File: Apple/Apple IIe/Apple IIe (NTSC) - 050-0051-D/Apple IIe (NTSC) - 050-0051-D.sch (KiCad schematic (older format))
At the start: 0 parts

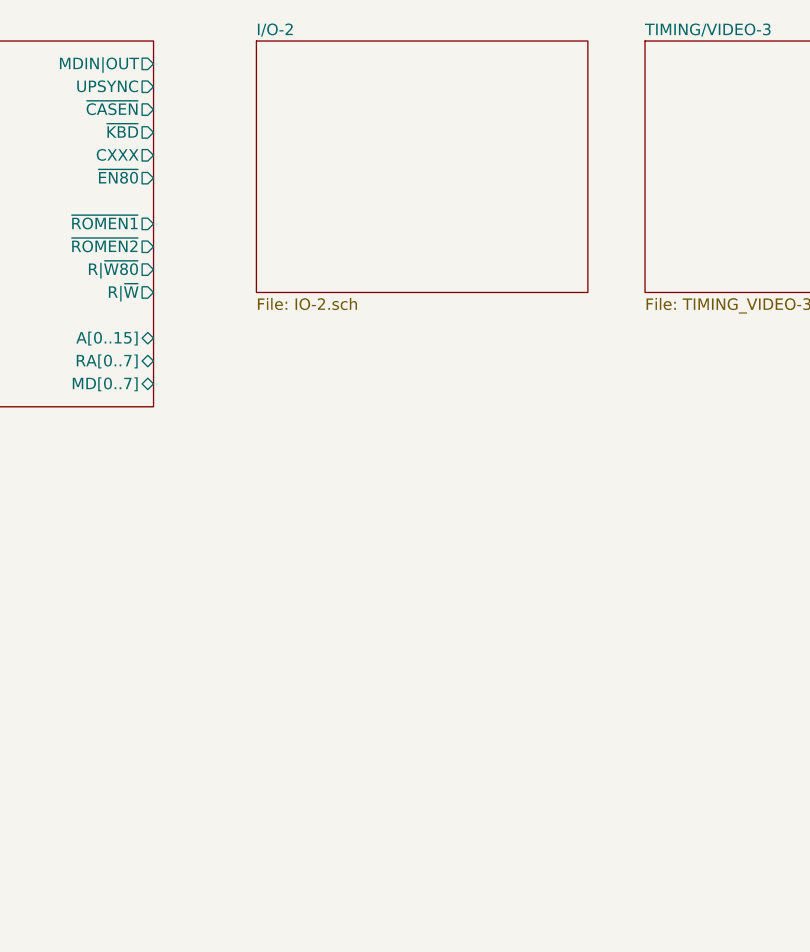
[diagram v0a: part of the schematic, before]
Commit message: Rough pass at I/O sheet
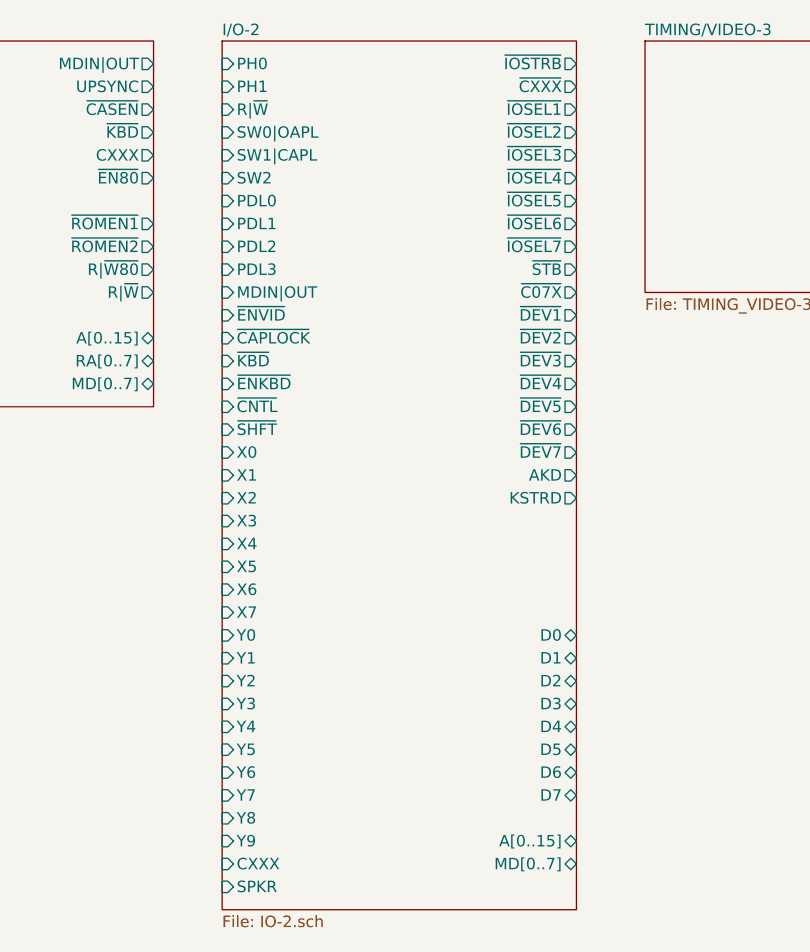
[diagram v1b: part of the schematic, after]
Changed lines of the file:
@@
 $EndSheet
 $Sheet
-S 3800 2800 1450 1100
+S 3650 2800 1550 3800
 U 60B91331
 F0 "I/O-2" 50
 F1 "IO-2.sch" 50
+F2 "SW2" I L 3650 3400 50
+F3 "SW1|CAPL" I L 3650 3300 50
+F4 "SW0|OAPL" I L 3650 3200 50
+F5 "~IOSTRB" O R 5200 2900 50
+F6 "~CXXX" O R 5200 3000 50
+F7 "~IOSEL1" O R 5200 3100 50
+F8 "~IOSEL2" O R 5200 3200 50
+F9 "~IOSEL3" O R 5200 3300 50
+F10 "~IOSEL4" O R 5200 3400 50
+F11 "~IOSEL5" O R 5200 3500 50
+F12 "~IOSEL6" O R 5200 3600 50
+F13 "~IOSEL7" O R 5200 3700 50
+F14 "~STB" O R 5200 3800 50
+F15 "~C07X" O R 5200 3900 50
+F16 "~DEV1" O R 5200 4000 50
+F17 "~DEV2" O R 5200 4100 50
+F18 "~DEV3" O R 5200 4200 50
+F19 "~DEV4" O R 5200 4300 50
+F20 "~DEV5" O R 5200 4400 50
+F21 "~DEV6" O R 5200 4500 50
+F22 "~DEV7" O R 5200 4600 50
+F23 "PDL0" I L 3650 3500 50
+F24 "PDL1" I L 3650 3600 50
+F25 "PDL2" I L 3650 3700 50
+F26 "PDL3" I L 3650 3800 50
+F27 "PH0" I L 3650 2900 50
+F28 "R|~W" I L 3650 3100 50
+F29 "MDIN|OUT" I L 3650 3900 50
+F30 "~ENVID" I L 3650 4000 50
+F31 "~CAPLOCK" I L 3650 4100 50
+F32 "~KBD" I L 3650 4200 50
+F33 "~ENKBD" I L 3650 4300 50
+F34 "~CNTL" I L 3650 4400 50
+F35 "~SHFT" I L 3650 4500 50
+F36 "X7" I L 3650 5300 50
+F37 "X6" I L 3650 5200 50
+F38 "X5" I L 3650 5100 50
+F39 "X4" I L 3650 5000 50
+F40 "X3" I L 3650 4900 50
+F41 "X2" I L 3650 4800 50
+F42 "X1" I L 3650 4700 50
+F43 "X0" I L 3650 4600 50
+F44 "Y9" I L 3650 6300 50
+F45 "Y8" I L 3650 6200 50
+F46 "Y7" I L 3650 6100 50
+F47 "Y6" I L 3650 6000 50
+F48 "Y5" I L 3650 5900 50
+F49 "Y4" I L 3650 5800 50
+F50 "Y3" I L 3650 5700 50
+F51 "Y2" I L 3650 5600 50
+F52 "Y1" I L 3650 5500 50
+F53 "Y0" I L 3650 5400 50
+F54 "AKD" O R 5200 4700 50
+F55 "KSTRD" O R 5200 4800 50
+F56 "MD[0..7]" B R 5200 6400 50
+F57 "A[0..15]" B R 5200 6300 50
+F58 "PH1" I L 3650 3000 50
+F59 "CXXX" I L 3650 6400 50
+F60 "D0" B R 5200 5400 50
+F61 "D1" B R 5200 5500 50
+F62 "D2" B R 5200 5600 50
+F63 "D3" B R 5200 5700 50
+F64 "D4" B R 5200 5800 50
+F65 "D5" B R 5200 5900 50
+F66 "D6" B R 5200 6000 50
+F67 "D7" B R 5200 6100 50
+F68 "SPKR" I L 3650 6500 50
 $EndSheet
 $Sheet

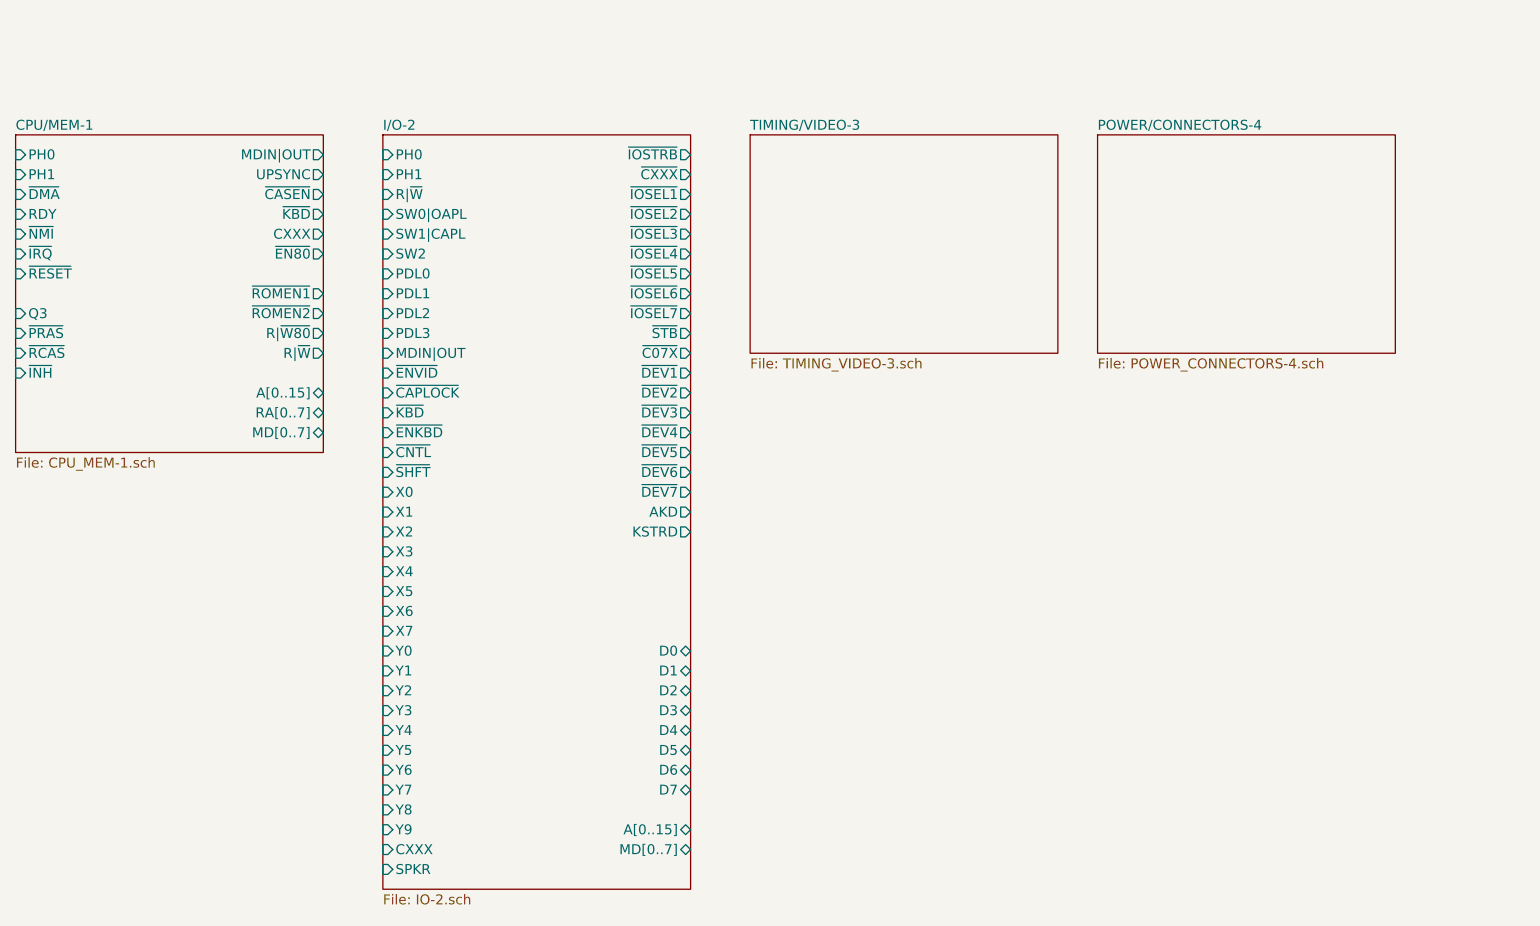
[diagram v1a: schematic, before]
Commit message: Rough pass at TIMING/VIDEO sheet
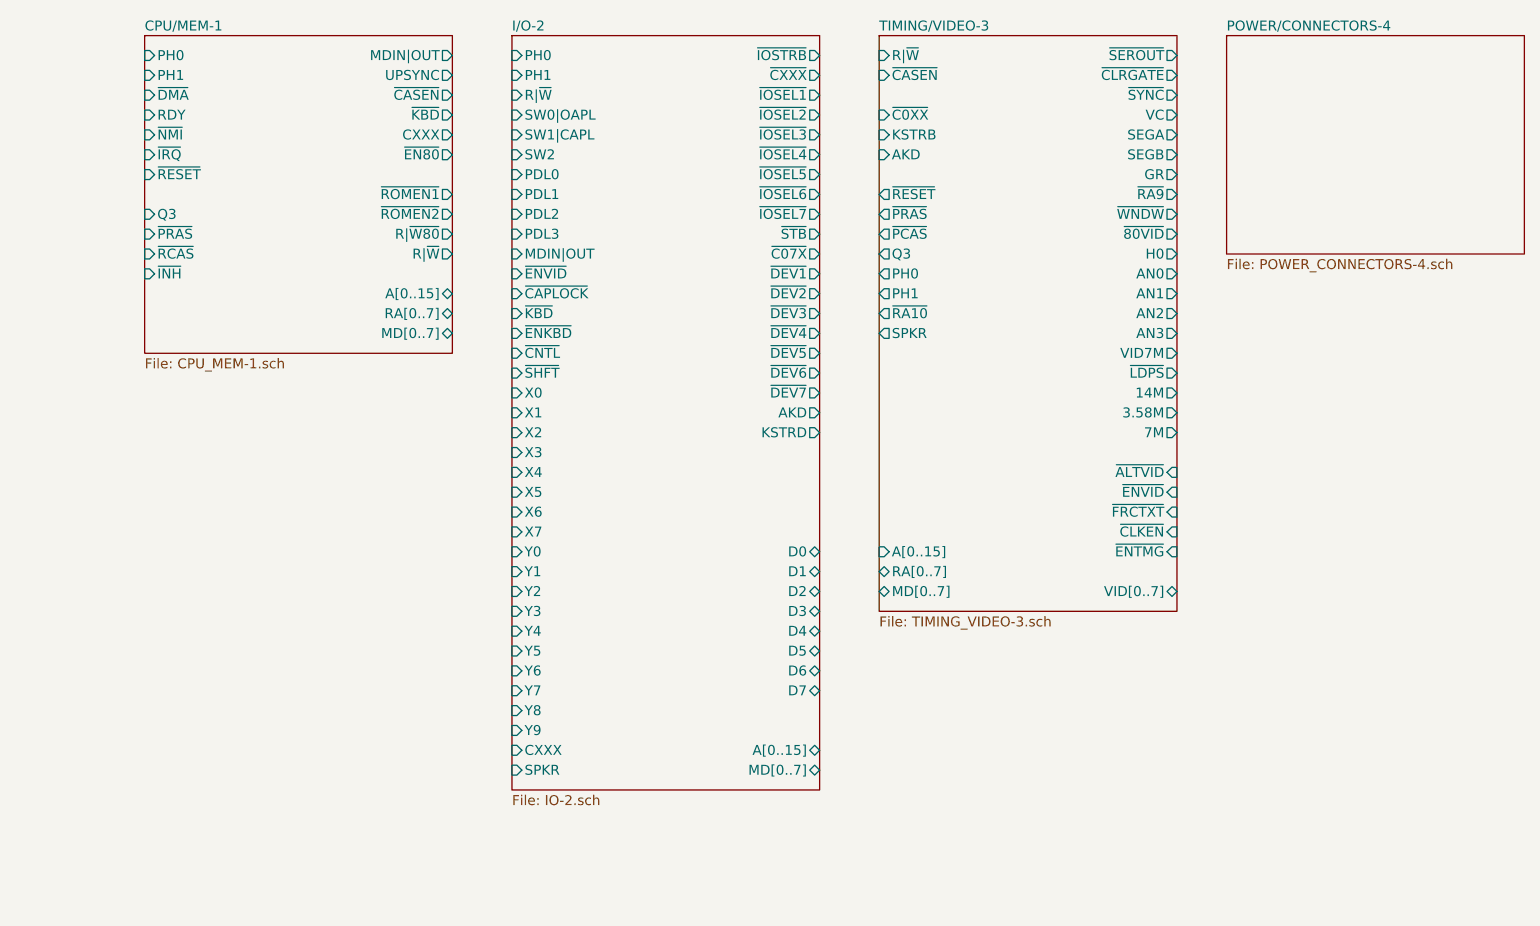
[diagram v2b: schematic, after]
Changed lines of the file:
@@
 $EndDescr
 $Sheet
-S 1800 2800 1550 1600
+S 2450 2300 1550 1600
 U 60B912AE
 F0 "CPU/MEM-1" 50
 F1 "CPU_MEM-1.sch" 50
-F2 "~RESET" I L 1800 3500 50
-F3 "~IRQ" I L 1800 3400 50
-F4 "~NMI" I L 1800 3300 50
-F5 "RDY" I L 1800 3200 50
-F6 "~DMA" I L 1800 3100 50
-F7 "RA[0..7]" B R 3350 4200 50
-F8 "PH0" I L 1800 2900 50
-F9 "Q3" I L 1800 3700 50
-F10 "~PRAS" I L 1800 3800 50
-F11 "~RCAS" I L 1800 3900 50
-F12 "~INH" I L 1800 4000 50
-F13 "R|~W" O R 3350 3900 50
-F14 "R|~W80" O R 3350 3800 50
-F15 "MD[0..7]" B R 3350 4300 50
-F16 "~ROMEN1" O R 3350 3600 50
-F17 "~ROMEN2" O R 3350 3700 50
-F18 "~EN80" O R 3350 3400 50
-F19 "CXXX" O R 3350 3300 50
-F20 "~KBD" O R 3350 3200 50
-F21 "~CASEN" O R 3350 3100 50
-F22 "UPSYNC" O R 3350 3000 50
-F23 "MDIN|OUT" O R 3350 2900 50
-F24 "A[0..15]" B R 3350 4100 50
-F25 "PH1" I L 1800 3000 50
+F2 "~RESET" I L 2450 3000 50
+F3 "~IRQ" I L 2450 2900 50
+F4 "~NMI" I L 2450 2800 50
+F5 "RDY" I L 2450 2700 50
+F6 "~DMA" I L 2450 2600 50
+F7 "RA[0..7]" B R 4000 3700 50
+F8 "PH0" I L 2450 2400 50
+F9 "Q3" I L 2450 3200 50
+F10 "~PRAS" I L 2450 3300 50
+F11 "~RCAS" I L 2450 3400 50
+F12 "~INH" I L 2450 3500 50
+F13 "R|~W" O R 4000 3400 50
+F14 "R|~W80" O R 4000 3300 50
+F15 "MD[0..7]" B R 4000 3800 50
+F16 "~ROMEN1" O R 4000 3100 50
+F17 "~ROMEN2" O R 4000 3200 50
+F18 "~EN80" O R 4000 2900 50
+F19 "CXXX" O R 4000 2800 50
+F20 "~KBD" O R 4000 2700 50
+F21 "~CASEN" O R 4000 2600 50
+F22 "UPSYNC" O R 4000 2500 50
+F23 "MDIN|OUT" O R 4000 2400 50
+F24 "A[0..15]" B R 4000 3600 50
+F25 "PH1" I L 2450 2500 50
 $EndSheet
 $Sheet
-S 3650 2800 1550 3800
+S 4300 2300 1550 3800
 U 60B91331
 F0 "I/O-2" 50
 F1 "IO-2.sch" 50
-F2 "SW2" I L 3650 3400 50
-F3 "SW1|CAPL" I L 3650 3300 50
-F4 "SW0|OAPL" I L 3650 3200 50
-F5 "~IOSTRB" O R 5200 2900 50
-F6 "~CXXX" O R 5200 3000 50
-F7 "~IOSEL1" O R 5200 3100 50
-F8 "~IOSEL2" O R 5200 3200 50
-F9 "~IOSEL3" O R 5200 3300 50
-F10 "~IOSEL4" O R 5200 3400 50
-F11 "~IOSEL5" O R 5200 3500 50
-F12 "~IOSEL6" O R 5200 3600 50
-F13 "~IOSEL7" O R 5200 3700 50
-F14 "~STB" O R 5200 3800 50
-F15 "~C07X" O R 5200 3900 50
-F16 "~DEV1" O R 5200 4000 50
-F17 "~DEV2" O R 5200 4100 50
-F18 "~DEV3" O R 5200 4200 50
-F19 "~DEV4" O R 5200 4300 50
-F20 "~DEV5" O R 5200 4400 50
-F21 "~DEV6" O R 5200 4500 50
-F22 "~DEV7" O R 5200 4600 50
-F23 "PDL0" I L 3650 3500 50
-F24 "PDL1" I L 3650 3600 50
-F25 "PDL2" I L 3650 3700 50
-F26 "PDL3" I L 3650 3800 50
-F27 "PH0" I L 3650 2900 50
-F28 "R|~W" I L 3650 3100 50
-F29 "MDIN|OUT" I L 3650 3900 50
-F30 "~ENVID" I L 3650 4000 50
-F31 "~CAPLOCK" I L 3650 4100 50
-F32 "~KBD" I L 3650 4200 50
-F33 "~ENKBD" I L 3650 4300 50
-F34 "~CNTL" I L 3650 4400 50
-F35 "~SHFT" I L 3650 4500 50
-F36 "X7" I L 3650 5300 50
-F37 "X6" I L 3650 5200 50
-F38 "X5" I L 3650 5100 50
-F39 "X4" I L 3650 5000 50
-F40 "X3" I L 3650 4900 50
-F41 "X2" I L 3650 4800 50
-F42 "X1" I L 3650 4700 50
-F43 "X0" I L 3650 4600 50
-F44 "Y9" I L 3650 6300 50
-F45 "Y8" I L 3650 6200 50
-F46 "Y7" I L 3650 6100 50
-F47 "Y6" I L 3650 6000 50
-F48 "Y5" I L 3650 5900 50
-F49 "Y4" I L 3650 5800 50
-F50 "Y3" I L 3650 5700 50
-F51 "Y2" I L 3650 5600 50
-F52 "Y1" I L 3650 5500 50
-F53 "Y0" I L 3650 5400 50
-F54 "AKD" O R 5200 4700 50
-F55 "KSTRD" O R 5200 4800 50
-F56 "MD[0..7]" B R 5200 6400 50
-F57 "A[0..15]" B R 5200 6300 50
-F58 "PH1" I L 3650 3000 50
-F59 "CXXX" I L 3650 6400 50
-F60 "D0" B R 5200 5400 50
-F61 "D1" B R 5200 5500 50
-F62 "D2" B R 5200 5600 50
-F63 "D3" B R 5200 5700 50
-F64 "D4" B R 5200 5800 50
-F65 "D5" B R 5200 5900 50
-F66 "D6" B R 5200 6000 50
-F67 "D7" B R 5200 6100 50
-F68 "SPKR" I L 3650 6500 50
+F2 "SW2" I L 4300 2900 50
+F3 "SW1|CAPL" I L 4300 2800 50
+F4 "SW0|OAPL" I L 4300 2700 50
+F5 "~IOSTRB" O R 5850 2400 50
+F6 "~CXXX" O R 5850 2500 50
+F7 "~IOSEL1" O R 5850 2600 50
+F8 "~IOSEL2" O R 5850 2700 50
+F9 "~IOSEL3" O R 5850 2800 50
+F10 "~IOSEL4" O R 5850 2900 50
+F11 "~IOSEL5" O R 5850 3000 50
+F12 "~IOSEL6" O R 5850 3100 50
+F13 "~IOSEL7" O R 5850 3200 50
+F14 "~STB" O R 5850 3300 50
+F15 "~C07X" O R 5850 3400 50
+F16 "~DEV1" O R 5850 3500 50
+F17 "~DEV2" O R 5850 3600 50
+F18 "~DEV3" O R 5850 3700 50
+F19 "~DEV4" O R 5850 3800 50
+F20 "~DEV5" O R 5850 3900 50
+F21 "~DEV6" O R 5850 4000 50
+F22 "~DEV7" O R 5850 4100 50
+F23 "PDL0" I L 4300 3000 50
+F24 "PDL1" I L 4300 3100 50
+F25 "PDL2" I L 4300 3200 50
+F26 "PDL3" I L 4300 3300 50
+F27 "PH0" I L 4300 2400 50
+F28 "R|~W" I L 4300 2600 50
+F29 "MDIN|OUT" I L 4300 3400 50
+F30 "~ENVID" I L 4300 3500 50
+F31 "~CAPLOCK" I L 4300 3600 50
+F32 "~KBD" I L 4300 3700 50
+F33 "~ENKBD" I L 4300 3800 50
+F34 "~CNTL" I L 4300 3900 50
+F35 "~SHFT" I L 4300 4000 50
+F36 "X7" I L 4300 4800 50
+F37 "X6" I L 4300 4700 50
+F38 "X5" I L 4300 4600 50
+F39 "X4" I L 4300 4500 50
+F40 "X3" I L 4300 4400 50
+F41 "X2" I L 4300 4300 50
+F42 "X1" I L 4300 4200 50
+F43 "X0" I L 4300 4100 50
+F44 "Y9" I L 4300 5800 50
+F45 "Y8" I L 4300 5700 50
+F46 "Y7" I L 4300 5600 50
+F47 "Y6" I L 4300 5500 50
+F48 "Y5" I L 4300 5400 50
+F49 "Y4" I L 4300 5300 50
+F50 "Y3" I L 4300 5200 50
+F51 "Y2" I L 4300 5100 50
+F52 "Y1" I L 4300 5000 50
+F53 "Y0" I L 4300 4900 50
+F54 "AKD" O R 5850 4200 50
+F55 "KSTRD" O R 5850 4300 50
+F56 "MD[0..7]" B R 5850 6000 50
+F57 "A[0..15]" B R 5850 5900 50
+F58 "PH1" I L 4300 2500 50
+F59 "CXXX" I L 4300 5900 50
+F60 "D0" B R 5850 4900 50
+F61 "D1" B R 5850 5000 50
+F62 "D2" B R 5850 5100 50
+F63 "D3" B R 5850 5200 50
+F64 "D4" B R 5850 5300 50
+F65 "D5" B R 5850 5400 50
+F66 "D6" B R 5850 5500 50
+F67 "D7" B R 5850 5600 50
+F68 "SPKR" I L 4300 6000 50
 $EndSheet
 $Sheet
-S 5500 2800 1550 1100
-U 60B9137B
-F0 "TIMING/VIDEO-3" 50
-F1 "TIMING_VIDEO-3.sch" 50
-$EndSheet
-$Sheet
-S 7250 2800 1500 1100
+S 7900 2300 1500 1100
 U 60B913A5
 F0 "POWER/CONNECTORS-4" 50
 F1 "POWER_CONNECTORS-4.sch" 50
 $EndSheet
+$Sheet
+S 6150 2300 1500 2900
+U 60B9137B
+F0 "TIMING/VIDEO-3" 50
+F1 "TIMING_VIDEO-3.sch" 50
+F2 "~ALTVID" I R 7650 4500 50
+F3 "~ENVID" I R 7650 4600 50
+F4 "MD[0..7]" B L 6150 5100 50
+F5 "R|~W" I L 6150 2400 50
+F6 "~C0XX" I L 6150 2700 50
+F7 "KSTRB" I L 6150 2800 50
+F8 "AKD" I L 6150 2900 50
+F9 "~FRCTXT" I R 7650 4700 50
+F10 "~CASEN" I L 6150 2500 50
+F11 "~CLRGATE" O R 7650 2500 50
+F12 "~SYNC" O R 7650 2600 50
+F13 "VC" O R 7650 2700 50
+F14 "SPKR" O L 6150 3800 50
+F15 "SEGB" O R 7650 2900 50
+F16 "SEGA" O R 7650 2800 50
+F17 "GR" O R 7650 3000 50
+F18 "~RA10" O L 6150 3700 50
+F19 "~RA9" O R 7650 3100 50
+F20 "~WNDW" O R 7650 3200 50
+F21 "~80VID" O R 7650 3300 50
+F22 "RA[0..7]" B L 6150 5000 50
+F23 "H0" O R 7650 3400 50
+F24 "AN0" O R 7650 3500 50
+F25 "AN1" O R 7650 3600 50
+F26 "AN2" O R 7650 3700 50
+F27 "AN3" O R 7650 3800 50
+F28 "~RESET" O L 6150 3100 50
+F29 "VID7M" O R 7650 3900 50
+F30 "~LDPS" O R 7650 4000 50
+F31 "~PRAS" O L 6150 3200 50
+F32 "~PCAS" O L 6150 3300 50
+F33 "Q3" O L 6150 3400 50
+F34 "PH1" O L 6150 3600 50
+F35 "PH0" O L 6150 3500 50
+F36 "14M" O R 7650 4100 50
+F37 "3.58M" O R 7650 4200 50
+F38 "7M" O R 7650 4300 50
+F39 "~CLKEN" I R 7650 4800 50
+F40 "~ENTMG" I R 7650 4900 50
+F41 "A[0..15]" I L 6150 4900 50
+F42 "~SEROUT" O R 7650 2400 50
+F43 "VID[0..7]" B R 7650 5100 50
+$EndSheet
 $EndSCHEMATC
